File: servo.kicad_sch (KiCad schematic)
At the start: 19 parts, among them J30 Screw_Terminal_01x02, J31 Conn_04x03_Servo, J32 Conn_04x03_Servo, J33 Conn_04x03_Servo, J34 Conn_04x03_Servo, U4 PCA9685PW

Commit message: Redesign for SMD and new pinmap
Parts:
- J30: footprint TerminalBlock:TerminalBlock_bornier-2_P5.08mm -> Phoenix_MSTBA:MSTBA-2,5-2-G-5,08
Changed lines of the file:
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@@
       (effects (font (size 1.27 1.27)))
     )
-    (property "Footprint" "TerminalBlock:TerminalBlock_bornier-2_P5.08mm" (at 41.91 86.36 0)
+    (property "Footprint" "Phoenix_MSTBA:MSTBA-2,5-2-G-5,08" (at 41.91 86.36 0)
       (effects (font (size 1.27 1.27)) hide)
     )

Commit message: Re-arrange pca
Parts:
- removed JP1, JP2, JP3, JP4, JP5, JP6: SolderJumper_2_Open, Jumper:SolderJumper-2_P1.3mm_Open_RoundedPad1.0x1.5mm, symbol Jumper:SolderJumper_2_Open

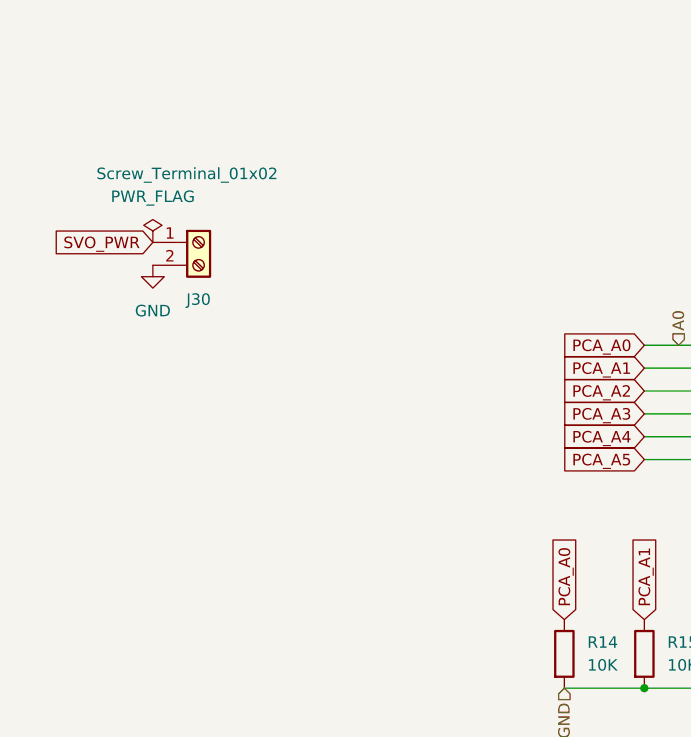
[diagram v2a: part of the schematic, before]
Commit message: Add servo power indicator
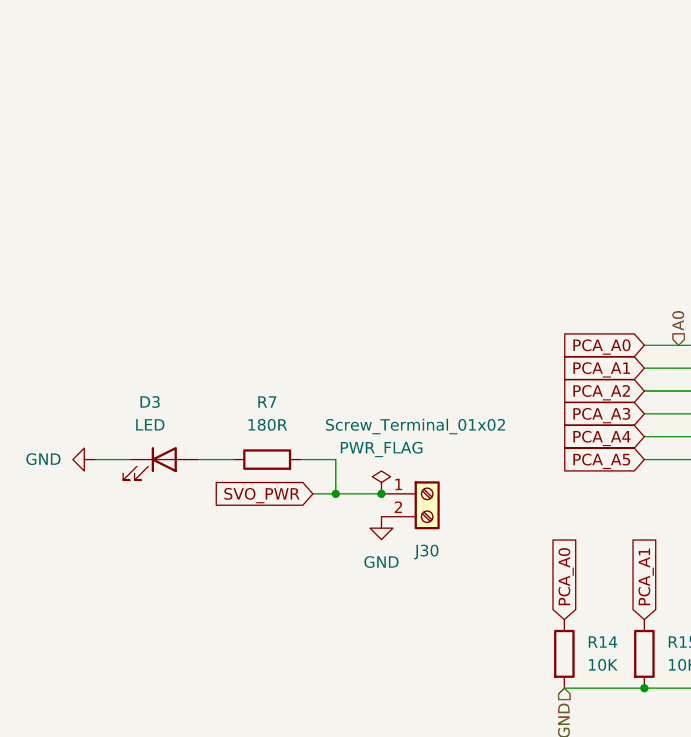
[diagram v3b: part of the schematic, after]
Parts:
- added D3: LED, LED_SMD:LED_0805_2012Metric, symbol Device:LED
- added R7: 180R, Resistor_SMD:R_0805_2012Metric, symbol Device:R
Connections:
- net GND: now also D3.1 (K)
- net SVO_PWR: now also R7.2
- new net: D3.2 (A), R7.1
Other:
- moved on the sheet: J30

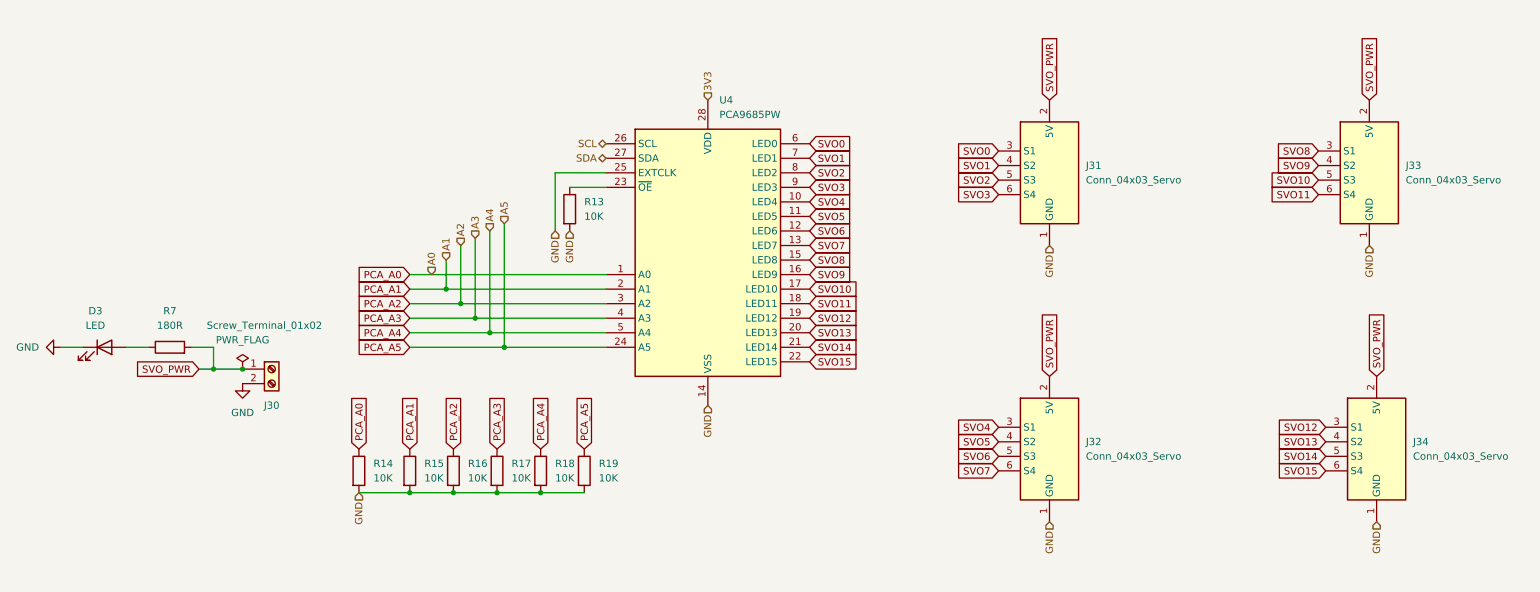
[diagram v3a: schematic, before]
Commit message: Fix global labels
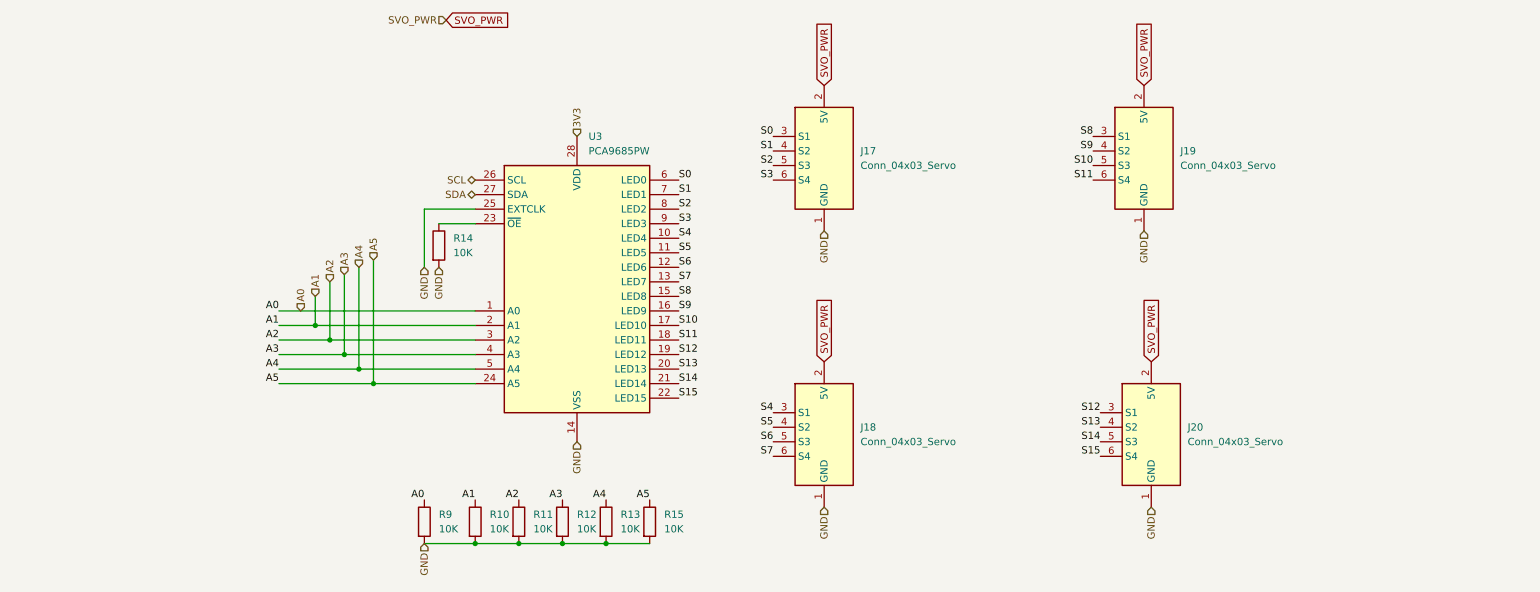
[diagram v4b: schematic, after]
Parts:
- removed D3: LED, LED_SMD:LED_0805_2012Metric, symbol Device:LED
- removed J30: Screw_Terminal_01x02, Phoenix_MSTBA:MSTBA-2,5-2-G-5,08, symbol Connector:Screw_Terminal_01x02
- removed R7: 180R, Resistor_SMD:R_0805_2012Metric, symbol Device:R
- renumbered J31 to J17, J32 to J18, J33 to J19, J34 to J20, R15 to R10, R16 to R11, R17 to R12, R18 to R13, R13 to R14, R19 to R15, R14 to R9, U4 to U3
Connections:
- net PCA_A0 renamed A0
- net PCA_A1 renamed A1
- net PCA_A2 renamed A2
- net PCA_A3 renamed A3
- net PCA_A4 renamed A4
- net PCA_A5 renamed A5
- net SVO0 renamed S0
- net SVO1 renamed S1
- net SVO10 renamed S10
- net SVO11 renamed S11
- net SVO12 renamed S12
- net SVO13 renamed S13
- net SVO14 renamed S14
- net SVO15 renamed S15
- net SVO2 renamed S2
- net SVO3 renamed S3
- net SVO4 renamed S4
- net SVO5 renamed S5
- net SVO6 renamed S6
- net SVO7 renamed S7
- net SVO8 renamed S8
- net SVO9 renamed S9
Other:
- moved on the sheet: J17, J18, J19, J20, R10, R11, R12, R13, R14, R15, R9, U3

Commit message: Almost finish 2nd pca
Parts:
- R10, R11, R12, R13, R14, R15, R9: footprint Resistor_SMD:R_1206_3216Metric -> Resistor_SMD:R_0603_1608Metric
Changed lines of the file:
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@@
 			)
 		)
-		(property "Footprint" "Resistor_SMD:R_1206_3216Metric"
+		(property "Footprint" "Resistor_SMD:R_0603_1608Metric"
 			(at 131.572 140.97 90)
 			(effects
@@
 			)
 		)
-		(property "Footprint" "Resistor_SMD:R_1206_3216Metric"
+		(property "Footprint" "Resistor_SMD:R_0603_1608Metric"
 			(at 116.332 140.97 90)
 			(effects
@@
 			)
 		)
-		(property "Footprint" "Resistor_SMD:R_1206_3216Metric"
+		(property "Footprint" "Resistor_SMD:R_0603_1608Metric"
 			(at 108.712 140.97 90)
 			(effects
@@
 			)
 		)
-		(property "Footprint" "Resistor_SMD:R_1206_3216Metric"
+		(property "Footprint" "Resistor_SMD:R_0603_1608Metric"
 			(at 123.952 140.97 90)
 			(effects
@@
 			)
 		)
-		(property "Footprint" "Resistor_SMD:R_1206_3216Metric"
+		(property "Footprint" "Resistor_SMD:R_0603_1608Metric"
 			(at 92.202 140.97 90)
 			(effects
@@
 			)
 		)
-		(property "Footprint" "Resistor_SMD:R_1206_3216Metric"
+		(property "Footprint" "Resistor_SMD:R_0603_1608Metric"
 			(at 101.092 140.97 90)
 			(effects
@@
 			)
 		)
-		(property "Footprint" "Resistor_SMD:R_1206_3216Metric"
+		(property "Footprint" "Resistor_SMD:R_0603_1608Metric"
 			(at 94.742 92.71 90)
 			(effects

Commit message: Add mfr part numbers and datasheets to all
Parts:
- J17, J18, J19, J20: Part Number (none) -> N/A
- R10, R11, R12, R13, R14, R15, R9: Part Number (none) -> RC0603FR-0710KL
- U3: LCSC C92206 -> (none); Part Number (none) -> PCA9685PW
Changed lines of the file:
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@@
 			)
 		)
-		(property "Datasheet" "~"
+		(property "Datasheet" "https://www.yageo.com/upload/media/product/products/datasheet/rchip/PYu-RC_Group_51_RoHS_L_12.pdf"
 			(at 133.35 140.97 0)
 			(effects
@@
 			)
 		)
+		(property "Part Number" "RC0603FR-0710KL"
+			(at 133.35 140.97 0)
+			(effects
+				(font
+					(size 1.27 1.27)
+				)
+				(hide yes)
+			)
+		)
 		(pin "1"
 		)
@@
 			)
 		)
-		(property "Datasheet" "~"
+		(property "Datasheet" "https://www.yageo.com/upload/media/product/products/datasheet/rchip/PYu-RC_Group_51_RoHS_L_12.pdf"
 			(at 118.11 140.97 0)
 			(effects
@@
 		)
 		(property "Description" "Resistor"
+			(at 118.11 140.97 0)
+			(effects
+				(font
+					(size 1.27 1.27)
+				)
+				(hide yes)
+			)
+		)
+		(property "Part Number" "RC0603FR-0710KL"
 			(at 118.11 140.97 0)
 			(effects
@@
 			)
 		)
-		(property "LCSC" "C92206"
+		(property "Part Number" "PCA9685PW"
 			(at 120.65 99.06 0)
 			(effects
@@
 		(on_board yes)
 		(dnp no)
+		(fields_autoplaced yes)
 		(property "Reference" "J17"
 			(at 170.18 76.1999 0)
@@
 			)
 		)
+		(property "Part Number" "N/A"
+			(at 160.02 82.55 0)
+			(effects
+				(font
+					(size 1.27 1.27)
+				)
+				(hide yes)
+			)
+		)
 		(pin "1"
 		)
@@
 			)
 		)
-		(property "Datasheet" "~"
+		(property "Datasheet" "https://www.yageo.com/upload/media/product/products/datasheet/rchip/PYu-RC_Group_51_RoHS_L_12.pdf"
 			(at 110.49 140.97 0)
 			(effects
@@
 			)
 		)
+		(property "Part Number" "RC0603FR-0710KL"
+			(at 110.49 140.97 0)
+			(effects
+				(font
+					(size 1.27 1.27)
+				)
+				(hide yes)
+			)
+		)
 		(pin "1"
 		)
@@
 			)
 		)
-		(property "Datasheet" "~"
+		(property "Datasheet" "https://www.yageo.com/upload/media/product/products/datasheet/rchip/PYu-RC_Group_51_RoHS_L_12.pdf"
 			(at 125.73 140.97 0)
 			(effects
@@
 			)
 		)
+		(property "Part Number" "RC0603FR-0710KL"
+			(at 125.73 140.97 0)
+			(effects
+				(font
+					(size 1.27 1.27)
+				)
+				(hide yes)
+			)
+		)
 		(pin "1"
 		)
@@
 			)
 		)
-		(property "Datasheet" "~"
+		(property "Datasheet" "https://www.yageo.com/upload/media/product/products/datasheet/rchip/PYu-RC_Group_51_RoHS_L_12.pdf"
 			(at 93.98 140.97 0)
 			(effects
@@
 			)
 		)
+		(property "Part Number" "RC0603FR-0710KL"
+			(at 93.98 140.97 0)
+			(effects
+				(font
+					(size 1.27 1.27)
+				)
+				(hide yes)
+			)
+		)
 		(pin "1"
 		)
@@
 			)
 		)
-		(property "Datasheet" "~"
+		(property "Datasheet" "https://www.yageo.com/upload/media/product/products/datasheet/rchip/PYu-RC_Group_51_RoHS_L_12.pdf"
 			(at 102.87 140.97 0)
 			(effects
@@
 		)
 		(property "Description" "Resistor"
+			(at 102.87 140.97 0)
+			(effects
+				(font
+					(size 1.27 1.27)
+				)
+				(hide yes)
+			)
+		)
+		(property "Part Number" "RC0603FR-0710KL"
 			(at 102.87 140.97 0)
 			(effects
@@
 			)
 		)
-		(property "Datasheet" "~"
+		(property "Datasheet" "https://www.yageo.com/upload/media/product/products/datasheet/rchip/PYu-RC_Group_51_RoHS_L_12.pdf"
 			(at 96.52 92.71 0)
 			(effects
@@
 		)
 		(property "Description" "Resistor"
+			(at 96.52 92.71 0)
+			(effects
+				(font
+					(size 1.27 1.27)
+				)
+				(hide yes)
+			)
+		)
+		(property "Part Number" "RC0603FR-0710KL"
 			(at 96.52 92.71 0)
 			(effects
@@
 			)
 		)
+		(property "Part Number" "N/A"
+			(at 215.9 82.55 0)
+			(effects
+				(font
+					(size 1.27 1.27)
+				)
+				(hide yes)
+			)
+		)
 		(pin "1"
 		)
@@
 			)
 		)
+		(property "Part Number" "N/A"
+			(at 217.17 130.81 0)
+			(effects
+				(font
+					(size 1.27 1.27)
+				)
+				(hide yes)
+			)
+		)
 		(pin "1"
 		)
@@
 			(at 160.02 130.81 0)
 			(effects
+				(font
+					(size 1.27 1.27)
+				)
+				(hide yes)
+			)
+		)
+		(property "Part Number" "N/A"
+			(at 160.02 130.81 0)
+			(effects
